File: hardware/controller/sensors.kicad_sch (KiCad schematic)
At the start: 10 parts, among them J4 Conn_01x07, U7 MPU-6050

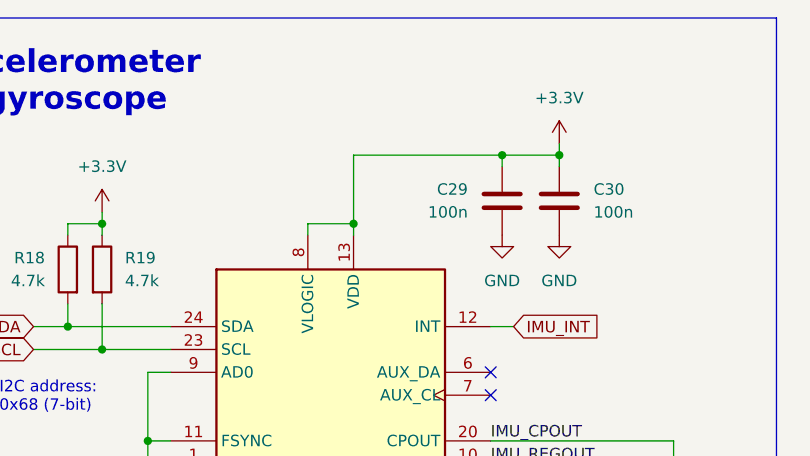
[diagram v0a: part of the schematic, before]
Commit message: full layout, edge power switch
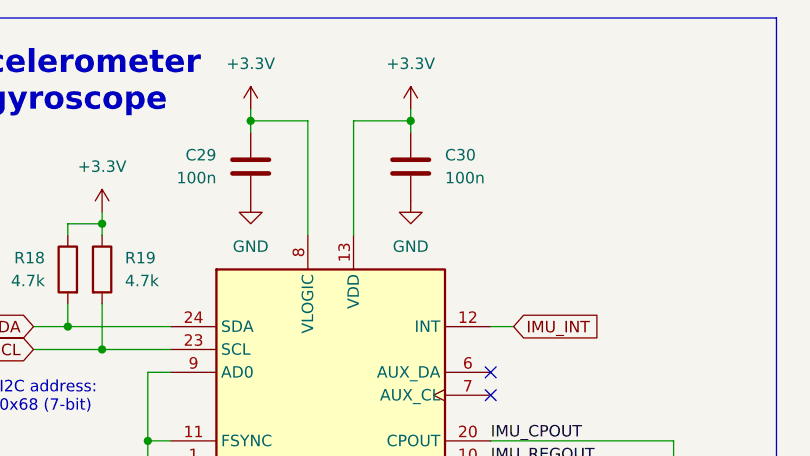
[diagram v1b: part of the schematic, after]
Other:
- moved on the sheet: C29, C30

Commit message: wip
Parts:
- added C77: 100n, Capacitor_SMD:C_0603_1608Metric, symbol Device:C
- added C78: 220n, Capacitor_SMD:C_0603_1608Metric, symbol Device:C
- added C79: 4.7u, Capacitor_SMD:C_0603_1608Metric, symbol Device:C
- added R50, R51: 4.7k, Resistor_SMD:R_0603_1608Metric, symbol Device:R
- added U20: HMC5883L, hogger2:HMC5883L_handsolder, symbol hogger2:HMC5883L
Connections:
- net +3.3V: now also C77.1, R50.1, R51.1, U20.13 (VDDIO), U20.2 (VDD), U20.4 (S1)
- net GND: now also C77.2, C79.2, U20.11 (GND), U20.9 (GND)
- new net MAG_C1: C79.1, U20.10 (C1)
- new net MAG_INT: U20.15 (DRDY)
- new net MAG_SCL: R51.2, U20.1 (SCL)
- new net MAG_SDA: R50.2, U20.16 (SDA)
- new net MAG_SETC: C78.2, U20.12 (SETC)
- new net MAG_SETP: C78.1, U20.8 (SETP)
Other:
- note added: "I2C address: 0x1E (7-bit)"
- note added: "magnetometer"
- moved on the sheet: C29, C30, C31, C32, C33, C34, J4, R18, R19, U7

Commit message: wip
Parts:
- renumbered C29 to C30, C30 to C31, C31 to C32, C32 to C33, C33 to C34, C34 to C35, C77 to C36, C78 to C37, C79 to C38, R50 to R20, R51 to R21, U7 to U6, U20 to U7

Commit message: wip elements
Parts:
- C32: value 10u -> 10u/50V; footprint Capacitor_SMD:C_0603_1608Metric -> Capacitor_SMD:C_1206_3216Metric
- C35: value 2n2 -> 2.2n
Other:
- moved on the sheet: C33
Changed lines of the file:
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@@
 	(title_block
 		(title "Hogger2 Controller")
-		(date "2025-02-22")
+		(date "2025-03-08")
 		(rev "V1.1")
 		(comment 4 "Author: Eryk Możdżeń")
@@
 	)
 	(junction
-		(at 172.72 58.42)
+		(at 173.99 58.42)
 		(diameter 0)
 		(color 0 0 0 0)
@@
 	(wire
 		(pts
-			(xy 158.75 58.42) (xy 172.72 58.42)
+			(xy 158.75 58.42) (xy 173.99 58.42)
 		)
 		(stroke
@@
 	(wire
 		(pts
+			(xy 173.99 58.42) (xy 199.39 58.42)
+		)
+		(stroke
+			(width 0)
+			(type default)
+		)
+	)
+	(wire
+		(pts
 			(xy 120.65 152.4) (xy 104.14 152.4)
 		)
@@
 	(wire
 		(pts
-			(xy 172.72 58.42) (xy 199.39 58.42)
-		)
-		(stroke
-			(width 0)
-			(type default)
-		)
-	)
-	(wire
-		(pts
 			(xy 90.17 132.08) (xy 90.17 133.35)
 		)
@@
 	(wire
 		(pts
-			(xy 172.72 58.42) (xy 172.72 59.69)
+			(xy 173.99 58.42) (xy 173.99 59.69)
 		)
 		(stroke
@@
 			)
 		)
-		(property "Value" "10u"
+		(property "Value" "10u/50V"
 			(at 162.56 64.7699 0)
 			(effects
@@
 			)
 		)
-		(property "Footprint" "Capacitor_SMD:C_0603_1608Metric"
+		(property "Footprint" "Capacitor_SMD:C_1206_3216Metric"
 			(at 159.7152 67.31 0)
 			(effects
@@
 	(symbol
 		(lib_id "power:GND")
-		(at 172.72 67.31 0)
+		(at 173.99 67.31 0)
 		(unit 1)
 		(exclude_from_sim no)
@@
 		(fields_autoplaced yes)
 		(property "Reference" "#PWR072"
-			(at 172.72 73.66 0)
+			(at 173.99 73.66 0)
 			(effects
 				(font
@@
 		)
 		(property "Value" "GND"
-			(at 172.72 72.39 0)
+			(at 173.99 72.39 0)
 			(effects
 				(font
@@
 		)
 		(property "Footprint" ""
-			(at 172.72 67.31 0)
+			(at 173.99 67.31 0)
 			(effects
 				(font
@@
 		)
 		(property "Datasheet" ""
-			(at 172.72 67.31 0)
+			(at 173.99 67.31 0)
 			(effects
 				(font
@@
 		)
 		(property "Description" "Power symbol creates a global label with name \"GND\" , ground"
-			(at 172.72 67.31 0)
+			(at 173.99 67.31 0)
 			(effects
 				(font
@@
 	(symbol
 		(lib_id "Device:C")
-		(at 172.72 63.5 0)
+		(at 173.99 63.5 0)
 		(unit 1)
 		(exclude_from_sim no)
@@
 		(dnp no)
 		(property "Reference" "C33"
-			(at 176.53 62.2299 0)
+			(at 177.8 62.2299 0)
 			(effects
 				(font
@@
 		)
 		(property "Value" "100n"
-			(at 176.53 64.7699 0)
+			(at 177.8 64.7699 0)
 			(effects
 				(font
@@
 		)
 		(property "Footprint" "Capacitor_SMD:C_0603_1608Metric"
-			(at 173.6852 67.31 0)
+			(at 174.9552 67.31 0)
 			(effects
 				(font
@@
 		)
 		(property "Datasheet" "~"
-			(at 172.72 63.5 0)
+			(at 173.99 63.5 0)
 			(effects
 				(font
@@
 		)
 		(property "Description" "Unpolarized capacitor"
-			(at 172.72 63.5 0)
+			(at 173.99 63.5 0)
 			(effects
 				(font
@@
 			)
 		)
-		(property "Value" "2n2"
+		(property "Value" "2.2n"
 			(at 138.43 88.8999 0)
 			(effects
